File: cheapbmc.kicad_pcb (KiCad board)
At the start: 2 copper layers, 57.2 x 48.9 mm, 17 parts, among them J1 Conn_01x03_Male, J2 atxpanel, J3 atxpanel, K1 SILxx-1Axx-71x, K2 SILxx-1Axx-71x, Q1 BC547, Q2 BC547, U1 NodeMCU1.0(ESP-12E), U2 FODM217A

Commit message: Add some mounting holes
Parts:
- added H1: MountingHole, MountingHole:MountingHole_3.2mm_M3, F.Cu at (111.8, 50.8)
- added H2: MountingHole, MountingHole:MountingHole_3.2mm_M3, F.Cu at (163.8, 76.2)
- added H3: MountingHole, MountingHole:MountingHole_3.2mm_M3, F.Cu at (111.8, 76.2)
- added H4: MountingHole, MountingHole:MountingHole_3.2mm_M3, F.Cu at (163.8, 50.8)
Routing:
- net PWRLED_N: track 74.0 -> 75.6 mm
- net PWRLED_P: track 68.0 -> 68.9 mm

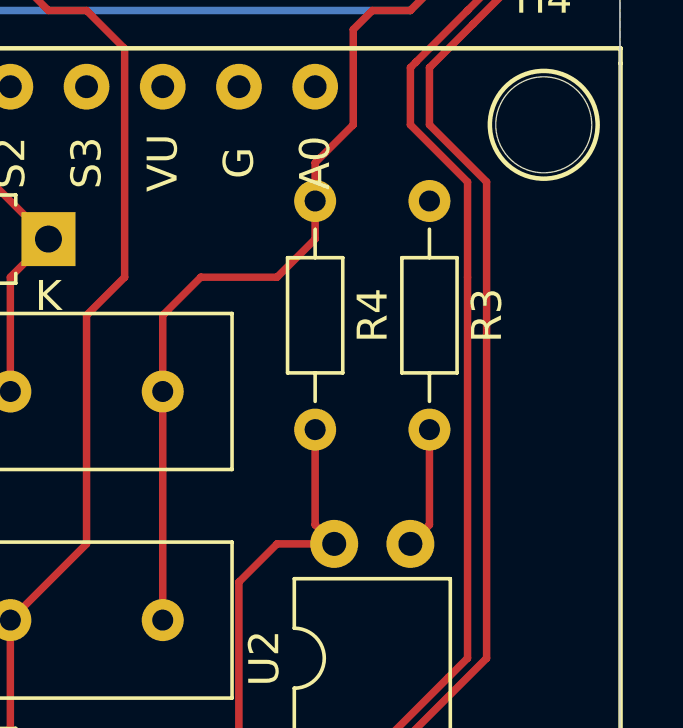
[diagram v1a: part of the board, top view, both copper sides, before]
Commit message: move R4 out of H4's courtyard
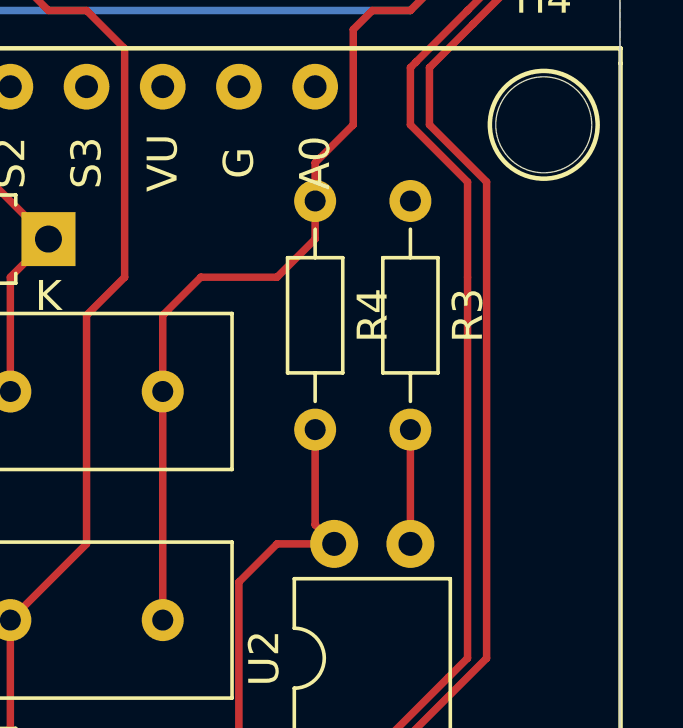
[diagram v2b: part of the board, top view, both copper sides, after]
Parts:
- moved R3 0.64 mm to (159.4, 53.3)
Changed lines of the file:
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@@
     (thickness 1.6)
     (drawings 9)
-    (tracks 166)
+    (tracks 165)
     (zones 0)
     (modules 21)
@@
   )
   (module Resistor_THT:R_Axial_DIN0204_L3.6mm_D1.6mm_P7.62mm_Horizontal (layer F.Cu)
-    (at 160.02 53.34 270)
+    (at 159.385 53.34 270)
     (descr "Resistor, Axial_DIN0204 series, Axial, Horizontal, pin pitch=7.62mm, 0.167W, length*diameter=3.6*1.6mm^2, http://cdn-reichelt.de/documents/datenblatt/B400/1_4W%23YAG.pdf")
     (tags "Resistor Axial_DIN0204 series Axial Horizontal pin pitch 7.62mm 0.167W length 3.6mm diameter 1.6mm")
@@
   (segment (start 127 68.58) (end 127 67.31) (width 0.25) (layer F.Cu) (net 21))
   (segment (start 125.73 69.85) (end 127 68.58) (width 0.25) (layer F.Cu) (net 21))
-  (segment (start 160.02 64.135) (end 159.385 64.77) (width 0.25) (layer F.Cu) (net 22))
-  (segment (start 160.02 60.96) (end 160.02 64.135) (width 0.25) (layer F.Cu) (net 22))
+  (segment (start 159.385 60.96) (end 159.385 64.77) (width 0.25) (layer F.Cu) (net 22))
   (segment (start 153.67 77.47) (end 153.67 66.04) (width 0.25) (layer F.Cu) (net 23))
   (segment (start 154.94 64.77) (end 156.845 64.77) (width 0.25) (layer F.Cu) (net 23))
@@
     (connect_pads (clearance 0.508))
     (min_thickness 0.254)
-    (fill (arc_segments 32) (thermal_gap 0.508) (thermal_bridge_width 0.508))
+    (fill yes (arc_segments 32) (thermal_gap 0.508) (thermal_bridge_width 0.508))
     (polygon
       (pts

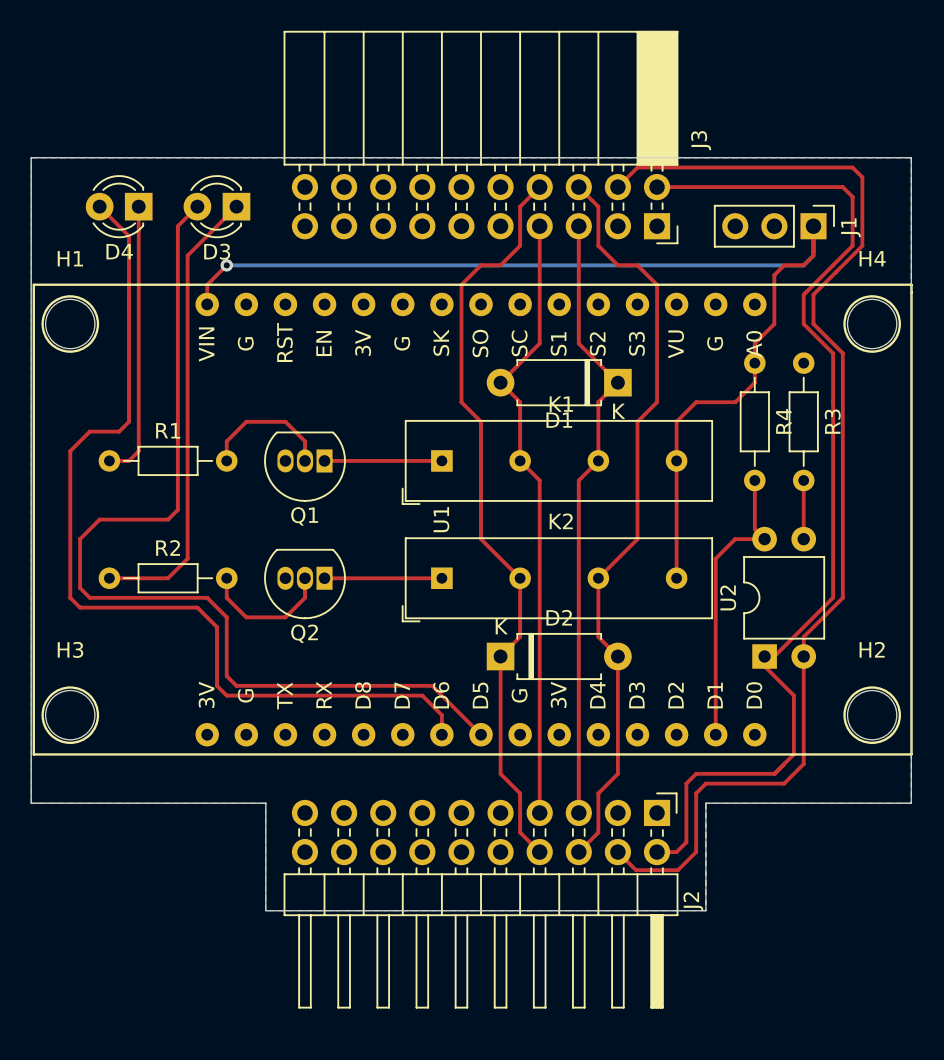
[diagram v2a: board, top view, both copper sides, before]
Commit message: Improve front-panel footprint, add git/build silk
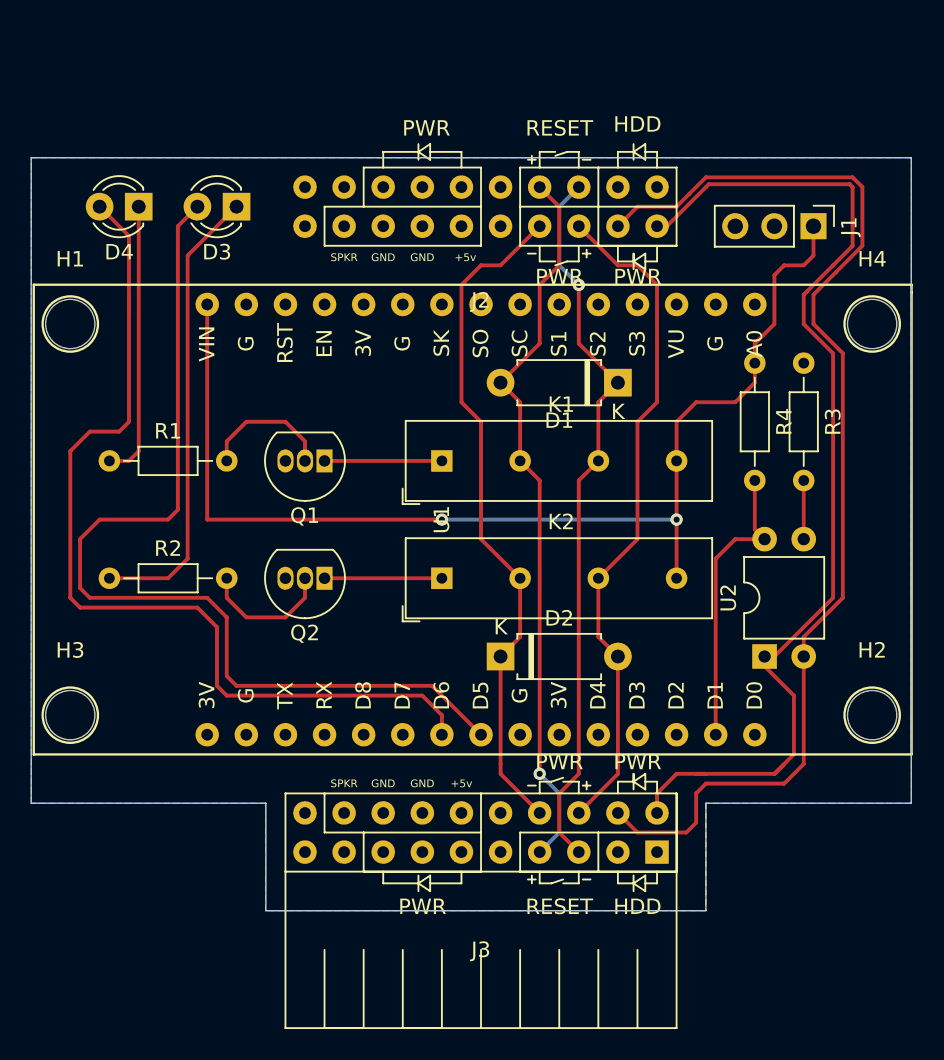
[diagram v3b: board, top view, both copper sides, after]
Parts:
- J2: footprint Connector_PinHeader_2.54mm:PinHeader_2x10_P2.54mm_Horizontal -> symbols:atx-panel
- J3: footprint Connector_PinSocket_2.54mm:PinSocket_2x10_P2.54mm_Horizontal -> symbols:atx-panel-horz-inverted
- moved J2 41.0 mm to (138.4, 43.2), turned to 180 degrees
- moved J3 41.0 mm to (138.4, 83.8), turned to 0 degrees
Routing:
- net RSTCON_N: track 40.2 -> 47.4 mm, vias 0 -> 1
- net RSTCON_P: track 40.2 -> 47.4 mm, vias 0 -> 1
- net PWRBTN_P: track 49.2 -> 44.1 mm
- net PWRBTN_N: track 49.2 -> 44.1 mm
- net PWRLED_N: track 75.6 -> 73.6 mm
- net +5V: track 72.1 -> 73.2 mm, vias 1 -> 2
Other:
- board text added: "BUILD_XXX"
- board text added: "GIT_XXXXX"

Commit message: Enlarge transistor footprints, correct relay footprint, add power selector switch, power LED/buttons
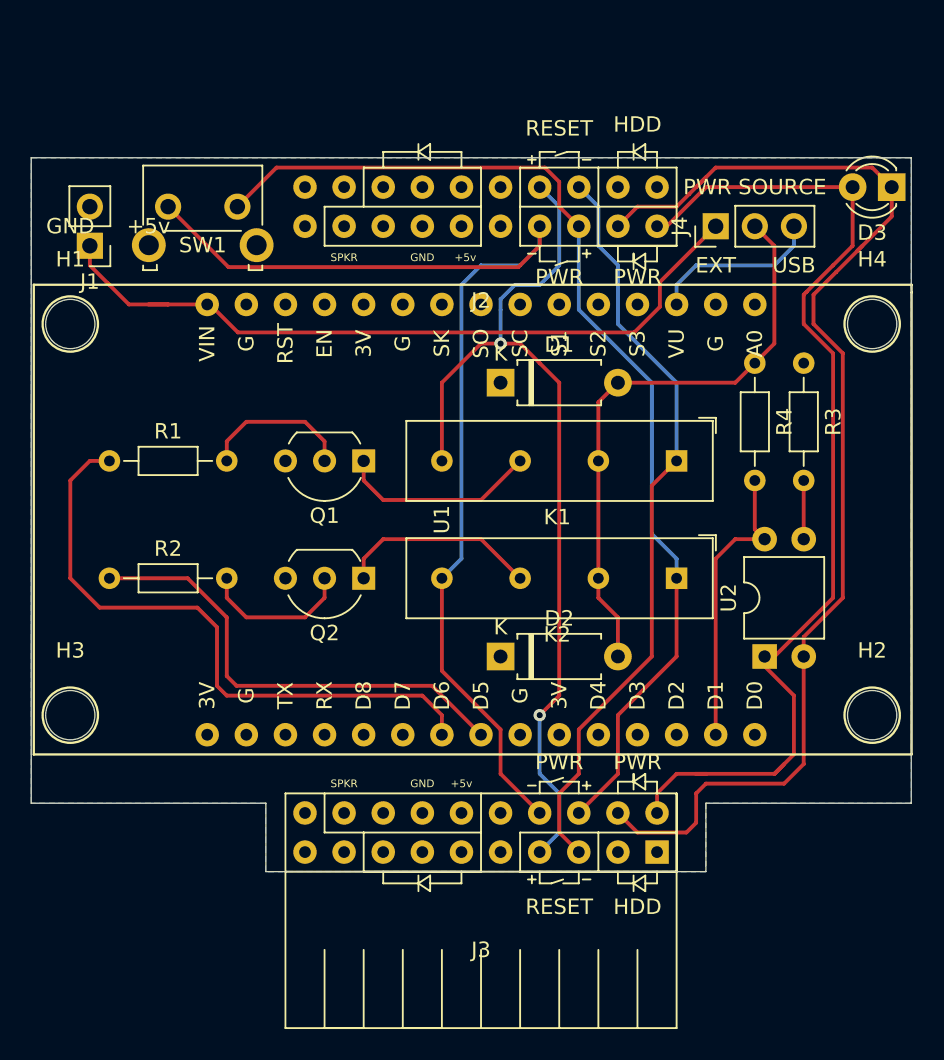
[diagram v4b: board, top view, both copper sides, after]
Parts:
- removed D4: LED, LED_THT:LED_D3.0mm
- added J4: Conn_01x03_Male, Connector_PinHeader_2.54mm:PinHeader_1x03_P2.54mm_Vertical, F.Cu at (153.7, 44.5)
- added SW1: SW_Push, Button_Switch_THT:SW_Tactile_SKHH_Angled, F.Cu at (118.1, 43.2)
- J1: value Conn_01x03_Male -> Conn_01x02_Male; footprint Connector_PinHeader_2.54mm:PinHeader_1x03_P2.54mm_Vertical -> Connector_PinHeader_2.54mm:PinHeader_1x02_P2.54mm_Vertical
- Q1, Q2: footprint Package_TO_SOT_THT:TO-92_Inline -> Package_TO_SOT_THT:TO-92_Inline_Wide
- moved J1 47.0 mm to (113.0, 45.7), turned to 180 degrees
- moved D3 42.6 mm to (165.1, 41.9)
- moved K1 15.2 mm to (151.1, 59.7), turned to 180 degrees
- moved K2 15.2 mm to (151.1, 67.3), turned to 180 degrees
- moved D1 7.62 mm to (139.7, 54.6), turned to 0 degrees
- moved Q1 2.54 mm to (130.8, 59.7)
- moved Q2 2.54 mm to (130.8, 67.3)
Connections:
- D1 pad 1: RSTCON_N -> GND
- D1 pad 2: RSTCON_P -> +5V
- D2 pad 1: PWRBTN_N -> GND
- D2 pad 2: PWRBTN_P -> +5V
- D3 pad 1: PWRBTN_TTL -> PWRLED_N
- D3 pad 2: Net-(D3-Pad2) -> PWRLED_P
- J1 pad 1: +5V -> Net-(J1-Pad1)
- J1 pad 2: Net-(J1-Pad2) -> GND
- K1 pad 1: Net-(K1-Pad1) -> RSTCON_N
- K1 pad 3: RSTCON_P -> +5V
- K1 pad 5: RSTCON_N -> Net-(K1-Pad5)
- K1 pad 7: +5V -> RSTCON_P
- K2 pad 1: Net-(K2-Pad1) -> PWRBTN_P
- K2 pad 3: PWRBTN_N -> +5V
- K2 pad 5: PWRBTN_P -> Net-(K2-Pad5)
- K2 pad 7: +5V -> PWRBTN_N
- Q1 pad 1: Net-(K1-Pad1) -> Net-(K1-Pad5)
- Q2 pad 1: Net-(K2-Pad1) -> Net-(K2-Pad5)
- U1 pad 15: +5V -> Net-(J1-Pad1)
- U1 pad 22: Net-(D4-Pad2) -> RSTCON_TTL
- U1 pad 23: Net-(D3-Pad2) -> PWRBTN_TTL
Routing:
- net Net-(D3-Pad2): track 62.7 -> 0.00 mm
- net Net-(D4-Pad2): track 61.8 -> 0.00 mm
- net Net-(J1-Pad1): track 0.00 -> 48.9 mm
- net +5V: track 73.2 -> 38.2 mm, vias 2 -> 0
- net PWRBTN_N: track 44.1 -> 72.4 mm
- net PWRBTN_P: track 44.1 -> 69.1 mm
- net RSTCON_TTL: track 18.0 -> 40.7 mm
- net Net-(K2-Pad5): track 0.00 -> 13.0 mm
- net Net-(K1-Pad5): track 0.00 -> 13.0 mm
- net RSTCON_P: track 47.4 -> 60.1 mm, vias 1 -> 2
- net Net-(J4-Pad3): track 0.00 -> 11.2 mm
- net Net-(K2-Pad1): track 7.62 -> 0.00 mm
- net Net-(K1-Pad1): track 7.62 -> 0.00 mm
- net PWRLED_N: track 73.6 -> 78.2 mm
- net RSTCON_N: track 47.4 -> 49.5 mm, vias 1 -> 0
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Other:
- board size 57.2 x 48.9 mm -> 57.2 x 46.4 mm
- board text added: "+5v"
- board text added: "EXT"
- board text added: "GND"
- board text added: "PWR SOURCE"
- board text added: "USB"
